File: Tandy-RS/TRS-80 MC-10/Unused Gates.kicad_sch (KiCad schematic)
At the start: 5 parts, among them U12 74LS14, U13 LS32, U18 74LS74, U19 74LS76, U20 LS32

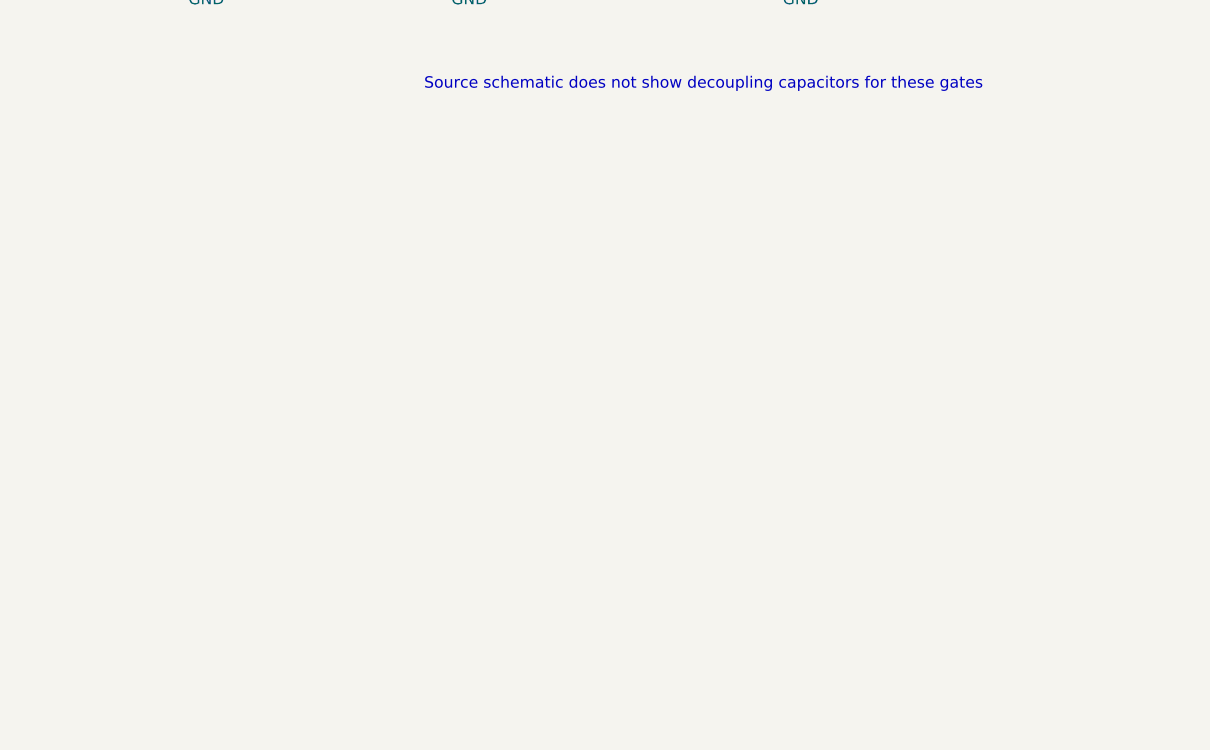
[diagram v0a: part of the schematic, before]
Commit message: erc, errors: 2, warnings: 0
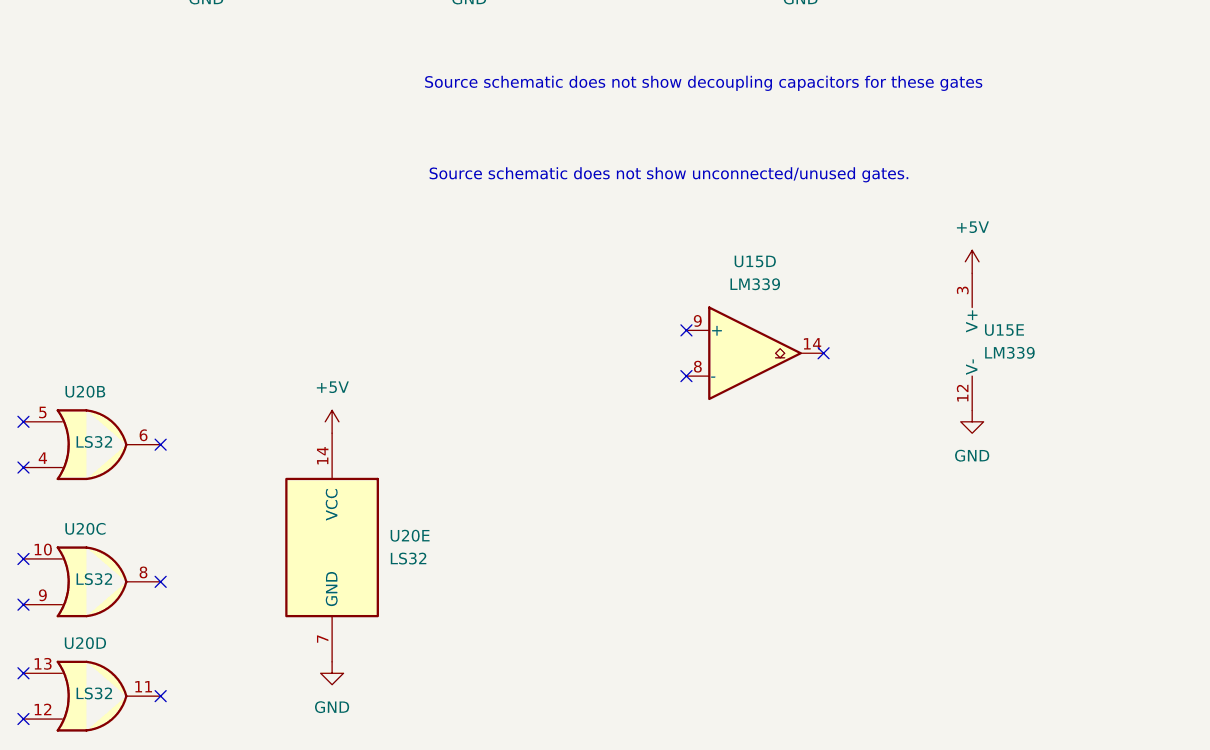
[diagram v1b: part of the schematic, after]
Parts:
- added U15: LM339, symbol Comparator:LM339
- added U20: LS32, symbol 74xx:74LS32
- added unit 3 of U20
- added unit 4 of U20
- added unit 2 of U20
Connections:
- net +5V: now also U15.3 (V+), U20.14 (VCC)
- net GND: now also U15.12 (V-), U20.7 (GND)
- no-connect marks 0 -> 12
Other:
- note added: "Source schematic does not show unconnected/unused gates."

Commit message: erc clean
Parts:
- removed unit 5 of U15
- removed U20: LS32, symbol 74xx:74LS32
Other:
- moved on the sheet: U12G, U13E, U18C, U19C, U20B, U20C, U20D, U20E
